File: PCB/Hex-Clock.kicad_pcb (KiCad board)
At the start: 2 copper layers, 77.1 x 89 mm, 21 parts

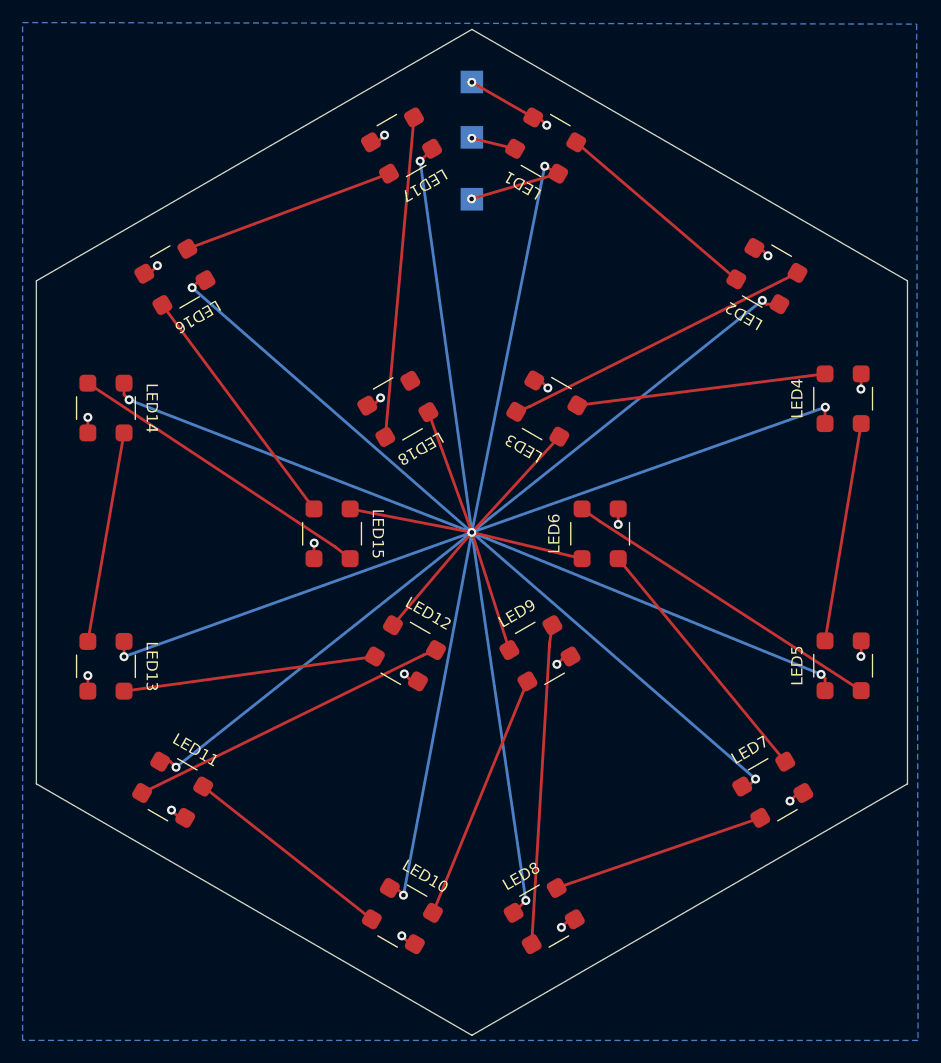
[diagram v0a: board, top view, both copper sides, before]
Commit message: Added LambBrainz silkscreen logo. Added alignment dot for LEDs on silkscreen. Modified some traces
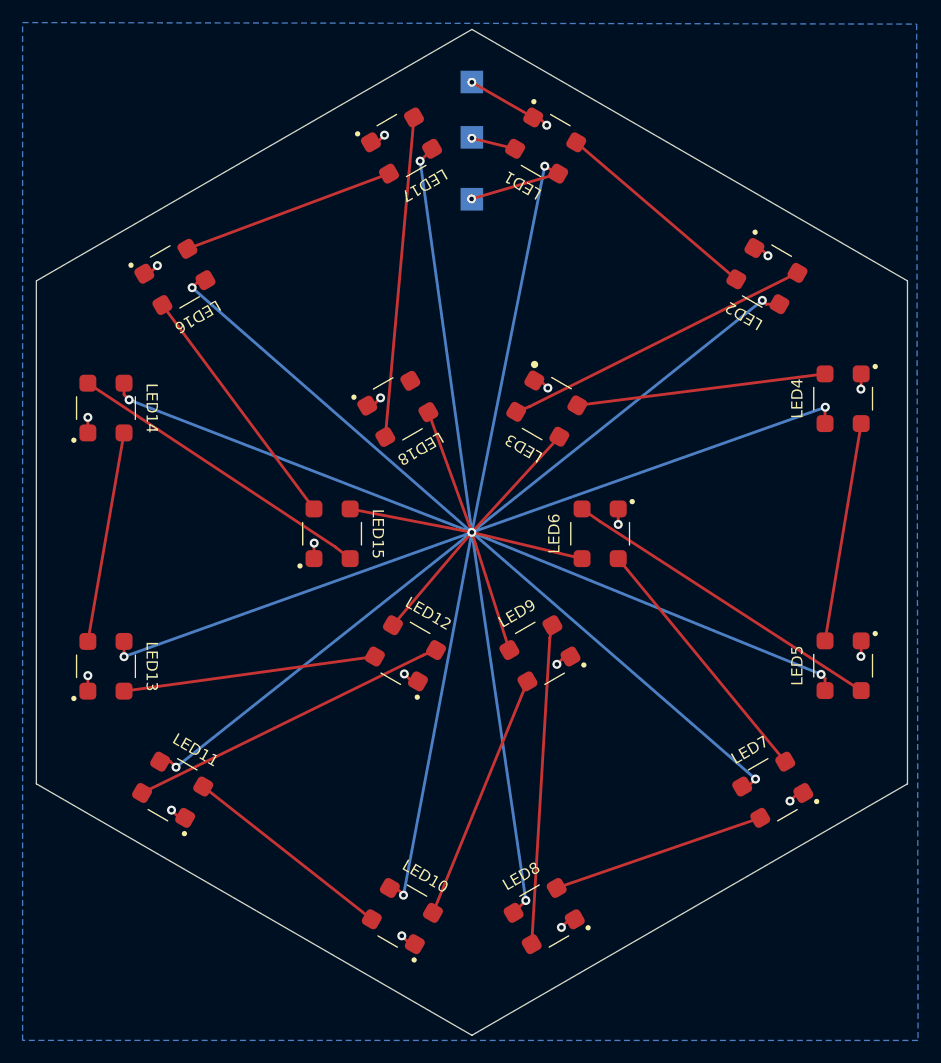
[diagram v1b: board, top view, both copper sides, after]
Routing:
- net +5V: track 488.1 -> 487.5 mm
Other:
- board text added: "LambBrainz.com"
